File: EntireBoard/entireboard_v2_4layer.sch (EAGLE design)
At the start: 52 parts, among them J1 FTSH-105-01-XXX-DV-K, P1 0532610271, U1 YKA, U2 RHD2216_QFN

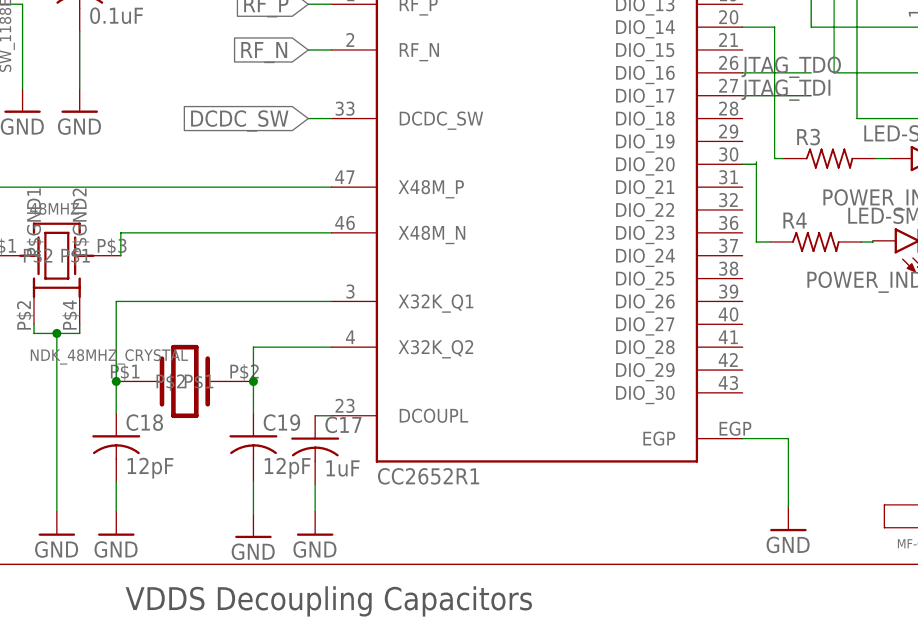
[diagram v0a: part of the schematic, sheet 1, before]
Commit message: drc for 4-layer
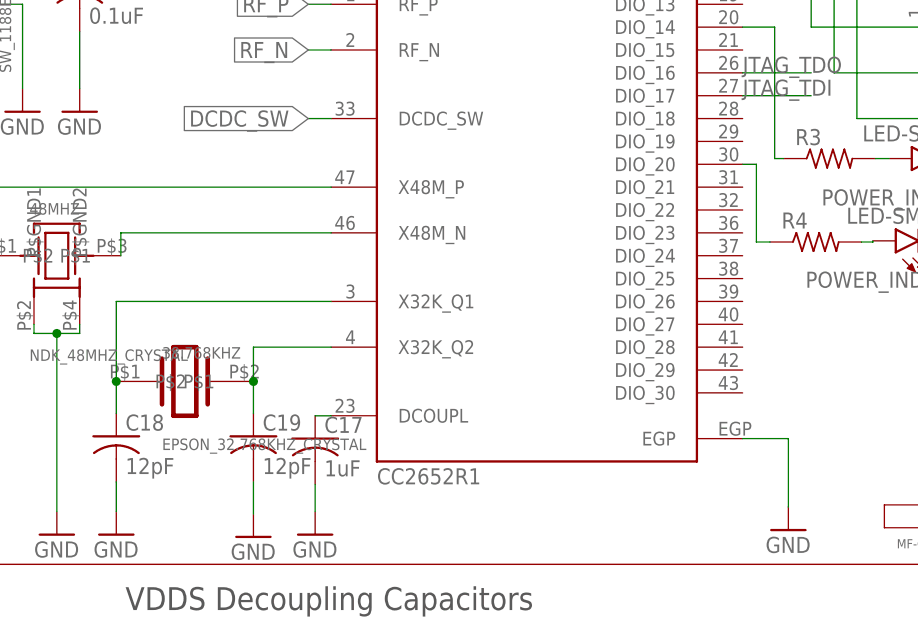
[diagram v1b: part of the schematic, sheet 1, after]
